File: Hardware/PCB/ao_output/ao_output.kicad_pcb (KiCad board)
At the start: 2 copper layers, 225 x 172.5 mm, 91 parts, among them J1 Conn_02x05_Odd_Even, J10 Synth_power_2x5, J11 Conn_02x05_Odd_Even, J12 Conn_01x17, J2 Conn_01x17, J3 AudioJack2, J4 AudioJack2, J5 AudioJack2, J6 AudioJack2, J7 AudioJack2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

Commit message: Rename file; PCB logos and text; more mounting holes
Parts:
- added GRAF3: AO logo, ao_tht:analogoutput, F.Cu at (114.0, 127.0)
- added GRAF4: OSHW logo, ao_tht:OSHW-Logo2_7.3x6mm_SilkScreen, F.Cu at (110.0, 43.5)
- added H5: MountingHole, ao_tht:MountingHole_3.2mm_M3, F.Cu at (-94.5, 15.5)
- added H6: MountingHole, ao_tht:MountingHole_3.2mm_M3, F.Cu at (-5.50, 15.5)
- added H7: MountingHole, ao_tht:MountingHole_3.2mm_M3, F.Cu at (-94.5, 134.5)
- added H8: MountingHole, ao_tht:MountingHole_3.2mm_M3, F.Cu at (-5.50, 134.5)
- U2: footprint ao_tht:DIP-14_W7.62mm_Socket_LongPads -> ao_tht:DIP-8_W7.62mm_Socket_LongPads
- U4: footprint Package_TO_SOT_THT:TO-92_Inline -> ao_tht:TO-92_Inline_Wide
- moved C10 251.6 mm to (44.5, 96.5), turned to 270 degrees
- moved U3 247.6 mm to (53.3, 73.7)
- moved C7 241.0 mm to (45.7, 81.3), turned to 180 degrees
- moved R28 235.0 mm to (59.7, 118.1), turned to 90 degrees
- moved R29 230.5 mm to (74.9, 152.4), turned to 90 degrees
- moved C9 228.5 mm to (61.0, 88.9)
- moved R30 221.0 mm to (59.7, 142.2), turned to 270 degrees
- moved R25 217.0 mm to (40.6, 118.1), turned to 90 degrees
- moved C8 214.0 mm to (61.0, 81.3)
- moved D8 210.8 mm to (59.7, 104.1), turned to 90 degrees
- moved C11 210.3 mm to (55.9, 96.5), turned to 270 degrees
- moved D1 207.6 mm to (69.8, 142.2), turned to 270 degrees
- moved D6 207.2 mm to (48.3, 104.1), turned to 90 degrees
- moved C13 206.3 mm to (60.2, 47.0)
- moved R17 205.6 mm to (77.5, 52.1)
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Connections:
- net /Power and panel/+12_IN renamed /Pot boards and power/+12_IN
- net /Power and panel/-12_IN renamed /Pot boards and power/-12_IN
- D1 pad 2: Net-(D1-Pad2) -> PHONESLX
- D2 pad 1: Net-(D1-Pad2) -> PHONESLX
- D3 pad 2: Net-(D3-Pad2) -> PHONESRX
- D4 pad 1: Net-(D3-Pad2) -> PHONESRX
- D5 pad 1: +12V -> +5V
- D5 pad 2: Net-(D5-Pad2) -> Net-(C10-Pad1)
- D6 pad 1: Net-(D5-Pad2) -> Net-(C10-Pad1)
- D6 pad 2: -12V -> GND
- D7 pad 1: +12V -> +5V
- D7 pad 2: Net-(D7-Pad2) -> Net-(C11-Pad1)
- D8 pad 1: Net-(D7-Pad2) -> Net-(C11-Pad1)
- D8 pad 2: -12V -> GND
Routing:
- net +12V: track 0.00 -> 203.1 mm
- net -12V: track 0.00 -> 168.5 mm
- net PHONESRX: track 0.00 -> 165.4 mm
- net PHONESLX: track 0.00 -> 135.4 mm
- net Net-(C5-Pad2): track 0.00 -> 99.2 mm
- net Net-(C6-Pad2): track 0.00 -> 92.6 mm
- net IN4A: track 0.00 -> 86.7 mm
- net IN1A: track 0.00 -> 85.2 mm
- net +5V: track 0.00 -> 82.2 mm
- net IN3A: track 0.00 -> 77.4 mm
- net IN2A: track 0.00 -> 75.9 mm
- net CH4X: track 0.00 -> 72.5 mm, vias 0 -> 1
- net CH1X: track 0.00 -> 64.6 mm
- net CH3X: track 0.00 -> 64.2 mm
- net PHONESLAX: track 0.00 -> 63.6 mm
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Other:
- board text added: "Rich Holmes / Mar 2021 CC0 1.0"
- board text added: "Stereo Output"

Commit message: rm Barton Daughterboard directory; final changes before fabbing; Gerbers; docs updates
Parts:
- C12, C13: footprint Capacitor_THT:CP_Radial_D5.0mm_P2.00mm -> ao_tht:CP_Radial_D6.3mm_P2.50mm
- C14, C15, C16, C17, C18, C19, C20: footprint Capacitor_THT:C_Disc_D3.0mm_W1.6mm_P2.50mm -> ao_tht:C_Disc_D3.0mm_W1.6mm_P2.50mm
- C7, C8, C9: footprint ao_tht:CP_Radial_D5.0mm_P2.00mm -> ao_tht:C_Radial_D5.0mm_H7.0mm_P2.00mm
- D1, D10, D2, D3, D4, D5, D6, D7, D8, D9: footprint Diode_THT:D_DO-41_SOD81_P7.62mm_Horizontal -> ao_tht:D_DO-41_SOD81_P7.62mm_Horizontal
- J1: footprint Connector_PinHeader_2.54mm:PinHeader_2x05_P2.54mm_Vertical -> Connector_PinSocket_2.54mm:PinSocket_2x05_P2.54mm_Vertical; moved to B.Cu
- R27, R28: value 75 -> 75R 1/2 W; footprint ao_tht:R_Axial_DIN0207_L6.3mm_D2.5mm_P10.16mm_Horizontal -> Resistor_THT:R_Axial_DIN0309_L9.0mm_D3.2mm_P12.70mm_Horizontal
- moved J11 71.4 mm to (-15.5, 87.5)
- moved GRAF4 70.5 mm to (100.3, 113.3)
- moved J1 23.0 mm to (115.5, 87.5), turned to 90 degrees
- moved D9 18.8 mm to (62.2, 15.5)
- moved C13 17.5 mm to (59.9, 29.5)
- moved C19 17.5 mm to (80.0, 26.9)
- moved C5 17.5 mm to (85.1, 29.5)
- moved U4 17.5 mm to (74.9, 26.9)
- moved C1 17.5 mm to (77.5, 65.0)
- moved C10 17.5 mm to (44.5, 79.0)
- moved C11 17.5 mm to (55.9, 79.0)
- moved C14 17.5 mm to (87.6, 68.9)
- moved C15 17.5 mm to (110.5, 68.9)
- moved C16 17.5 mm to (108.0, 32.0)
- moved C17 17.5 mm to (85.1, 39.6)
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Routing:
- net IN1A: track 85.2 -> 8.01 mm
- net IN3: track 8.74 -> 81.0 mm
- net IN4: track 31.5 -> 91.8 mm
- net IN2: track 15.3 -> 71.7 mm
- net IN2A: track 75.9 -> 22.8 mm
- net IN3A: track 77.4 -> 45.3 mm
- net IN1: track 39.9 -> 68.6 mm
- net IN3X: track 39.2 -> 62.3 mm
- net IN4X: track 63.2 -> 86.2 mm
- net IN1X: track 35.2 -> 58.2 mm
- net IN2X: track 61.3 -> 84.2 mm
- net IN4A: track 86.7 -> 67.7 mm
- net +12V: track 203.1 -> 221.7 mm
- net -12V: track 168.5 -> 187.0 mm
- net CH4LX: track 11.9 -> 29.5 mm
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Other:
- outline, holes or cut-outs redrawn

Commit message: Deletions
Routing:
- net PHONESLX: track 152.9 -> 153.4 mm

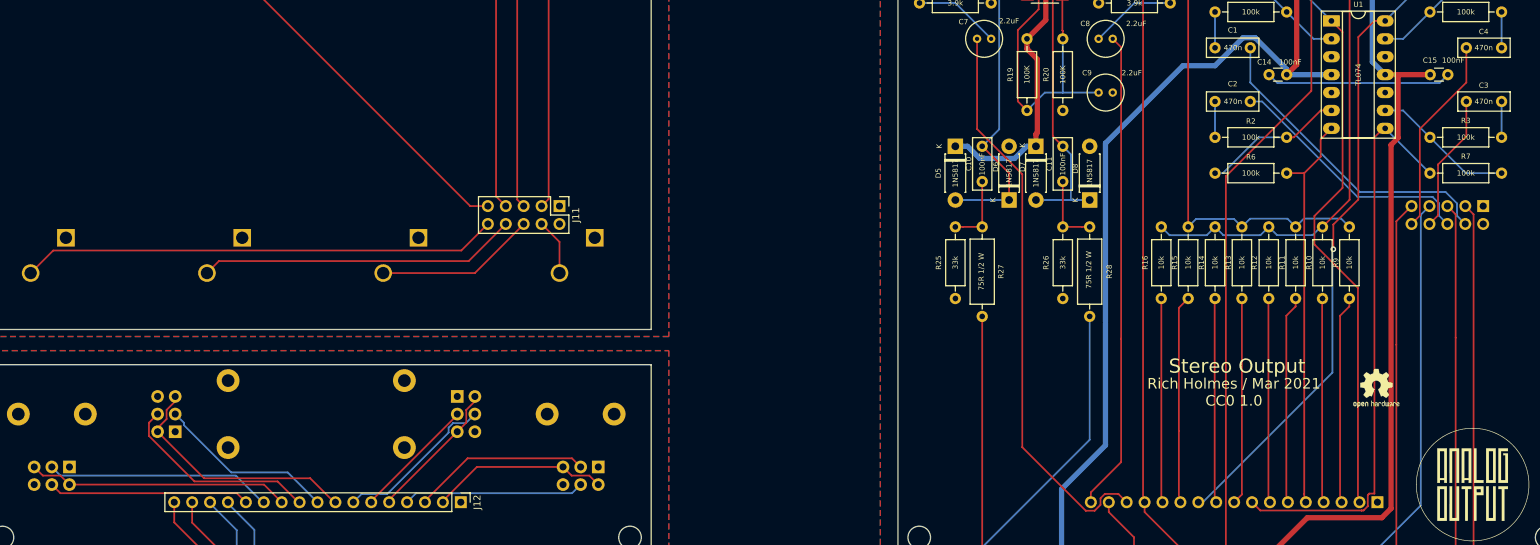
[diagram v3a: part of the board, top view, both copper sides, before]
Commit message: Reconnect pots, correct some values
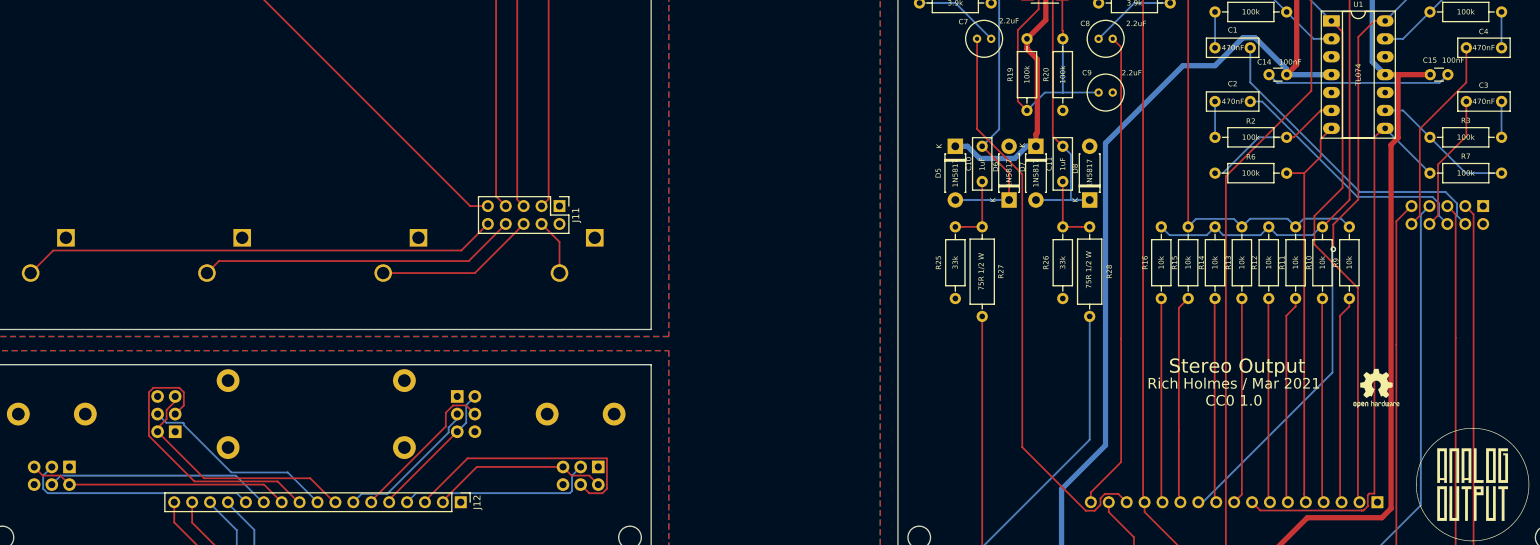
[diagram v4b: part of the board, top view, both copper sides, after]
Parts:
- C1, C2, C3, C4: value 470n -> 470nF
- C10, C11: value 100nF -> 1uF
- R19, R20: value 100K -> 100k
- RV1, RV2, RV3, RV4: value B100k -> A100k
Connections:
- RV5 pad 2: CH1L -> CH1R
- RV5 pad 5: CH1R -> CH1L
- RV6 pad 2: CH2L -> CH2R
- RV6 pad 5: CH2R -> CH2L
- RV7 pad 2: CH3L -> CH3R
- RV7 pad 5: CH3R -> CH3L
- RV8 pad 2: CH4L -> CH4R
- RV8 pad 5: CH4R -> CH4L
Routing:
- net CH1L: track 25.3 -> 37.3 mm
- net CH3R: track 28.9 -> 40.5 mm
- net CH4R: track 28.6 -> 33.1 mm
- net CH2L: track 17.6 -> 22.1 mm
- net CH3L: track 25.5 -> 28.0 mm
- net CH1R: track 25.7 -> 28.0 mm
- net CH2R: track 22.8 -> 20.7 mm

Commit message: Libraries cleanup; rm PCB layout and Gerbers; rm images of other headphone outputs; update README and schematic
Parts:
- removed C1, C2, C3, C4: 470nF, ao_tht:C_Rect_L7.2mm_W2.5mm_P5.00mm_FKS2_FKP2_MKS2_MKP2
- removed C10, C11: 1uF, ao_tht:C_Rect_L7.2mm_W2.5mm_P5.00mm_FKS2_FKP2_MKS2_MKP2
- removed C12, C13: 10uF, ao_tht:CP_Radial_D6.3mm_P2.50mm
- removed C14, C15, C16, C17, C19, C20: 100nF, ao_tht:C_Disc_D3.0mm_W1.6mm_P2.50mm
- removed C18: 330nF, ao_tht:C_Disc_D3.0mm_W1.6mm_P2.50mm
- removed C5, C6: 330pF, ao_tht:C_Disc_D3.0mm_W1.6mm_P2.50mm
- removed C7, C8, C9: 2.2uF, ao_tht:C_Radial_D5.0mm_H7.0mm_P2.00mm
- removed D1, D10, D2, D3, D4, D5, D6, D7, D8, D9: 1N5817, ao_tht:D_DO-41_SOD81_P7.62mm_Horizontal
- removed GRAF3: AO logo, ao_tht:analogoutput
- removed GRAF4: OSHW logo, ao_tht:OSHW-Logo2_7.3x6mm_SilkScreen
- removed H1, H2, H3, H4, H5, H6, H7, H8: MountingHole, ao_tht:MountingHole_3.2mm_M3
- removed J1: Conn_02x05_Odd_Even, Connector_PinSocket_2.54mm:PinSocket_2x05_P2.54mm_Vertical
- removed J10: Synth_power_2x5, ao_tht:Power_Header
- removed J11: Conn_02x05_Odd_Even, Connector_PinHeader_2.54mm:PinHeader_2x05_P2.54mm_Vertical
- removed J12: Conn_01x17, Connector_PinHeader_2.54mm:PinHeader_1x17_P2.54mm_Vertical
- removed J2: Conn_01x17, Connector_PinSocket_2.54mm:PinSocket_1x17_P2.54mm_Vertical
- removed J3, J4, J5, J6, J7, J8: AudioJack2, ao_tht:Jack_6.35mm_PJ_629HAN
- removed J9: AudioJack3, ao_tht:Jack_6.35mm_PJ_629HAN
- removed R1, R19, R2, R20, R3, R4, R5, R6, R7, R8: 100k, ao_tht:R_Axial_DIN0207_L6.3mm_D2.5mm_P10.16mm_Horizontal
- removed R10, R11, R12, R13, R14, R15, R16, R17, R18, R9: 10k, ao_tht:R_Axial_DIN0207_L6.3mm_D2.5mm_P10.16mm_Horizontal
- removed R21, R22, R23, R24: 3.9k, ao_tht:R_Axial_DIN0207_L6.3mm_D2.5mm_P10.16mm_Horizontal
- removed R25, R26: 33k, ao_tht:R_Axial_DIN0207_L6.3mm_D2.5mm_P10.16mm_Horizontal
- removed R27, R28: 75R 1/2 W, Resistor_THT:R_Axial_DIN0309_L9.0mm_D3.2mm_P12.70mm_Horizontal
- removed R29, R30: 1k, ao_tht:R_Axial_DIN0207_L6.3mm_D2.5mm_P10.16mm_Horizontal
- removed RV1, RV2, RV3, RV4: A100k, ao_tht:Potentiometer_Alpha_RA6020F_Single_Slide
- removed RV5, RV6, RV7, RV8, RV9: B10k, ao_tht:Potentiometer_Alpha_RD902F-40-00D_Dual_Vertical_CircularHoles_centered
- removed U1: TL074, ao_tht:DIP-14_W7.62mm_Socket_LongPads
- removed U2: TL072, ao_tht:DIP-8_W7.62mm_Socket_LongPads
- removed U3: LM4808, Package_SO:SOIC-8_3.9x4.9mm_P1.27mm
- removed U4: L78L05_TO92, ao_tht:TO-92_Inline_Wide
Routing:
- net +12V: track 221.7 -> 0.00 mm
- net -12V: track 187.0 -> 0.00 mm
- net PHONESRX: track 182.8 -> 0.00 mm
- net PHONESLX: track 153.4 -> 0.00 mm
- net Net-(C5-Pad2): track 99.2 -> 0.00 mm
- net Net-(C6-Pad2): track 92.6 -> 0.00 mm
- net IN4: track 91.8 -> 0.00 mm
- net CH4X: track 89.6 -> 0.00 mm, vias 1 -> 0
- net IN4X: track 86.2 -> 0.00 mm
- net IN2X: track 84.2 -> 0.00 mm
- net +5V: track 82.2 -> 0.00 mm
- net CH1X: track 82.2 -> 0.00 mm
- net CH3X: track 81.3 -> 0.00 mm
- net PHONESLAX: track 81.1 -> 0.00 mm
- net IN3: track 81.0 -> 0.00 mm
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- removed copper zone on B.Cu, net GND
- removed copper zone on F.Cu, net GND
- removed copper zone on B.Cu, net GND1
- removed copper zone on F.Cu, net GND1
- removed copper zone on B.Cu, net GND2
- removed copper zone on F.Cu, net GND2
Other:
- board outline removed
- board text removed: "Rich Holmes / Mar 2021 CC0 1.0"
- board text removed: "Stereo Output"
